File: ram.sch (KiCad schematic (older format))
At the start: 3 parts, among them U1 LFE5U-45F-6BG381C, U9 MT48LC4M16A2TG

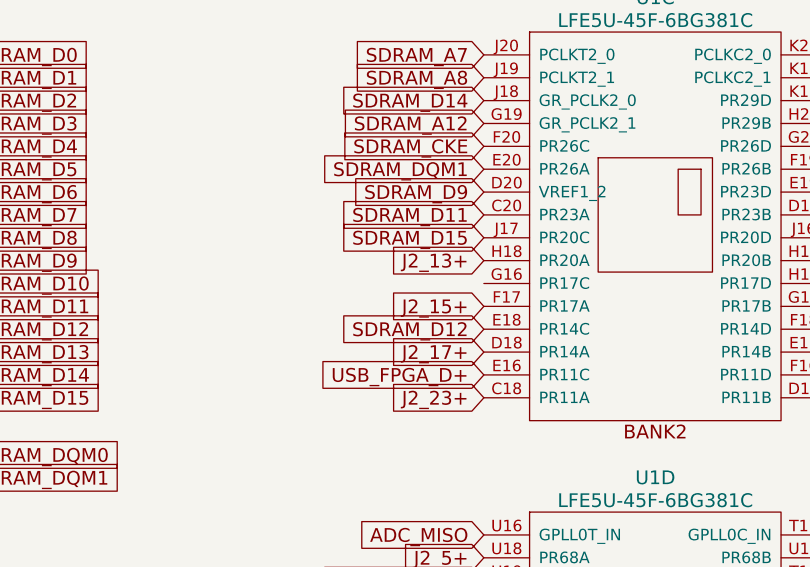
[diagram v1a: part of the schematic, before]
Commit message: schematics: connecting SHUTDOWN to FPGA
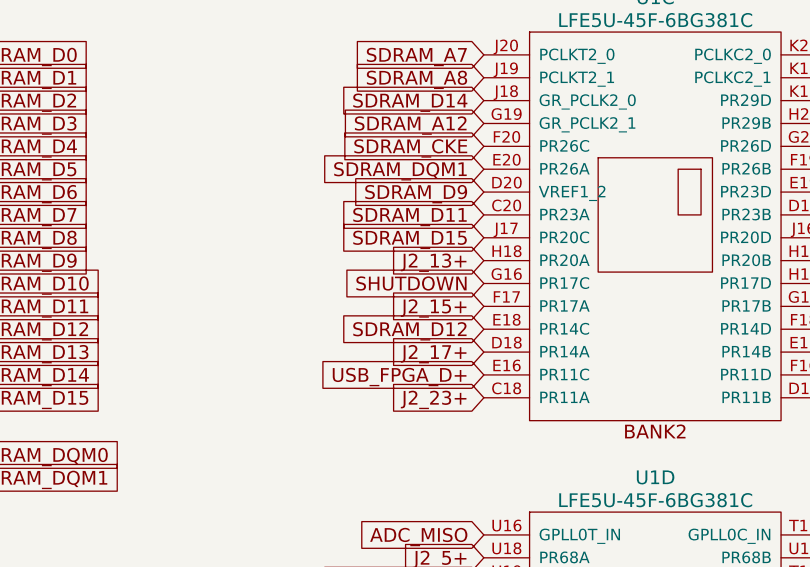
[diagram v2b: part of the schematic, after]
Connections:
- net SHUTDOWN: now reaches U1.G16 (PR17C)
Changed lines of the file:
@@
 	1    0    0    -1
 $EndComp
+Text GLabel 8550 3450 0    60   Input ~ 0
+SHUTDOWN
 $EndSCHEMATC

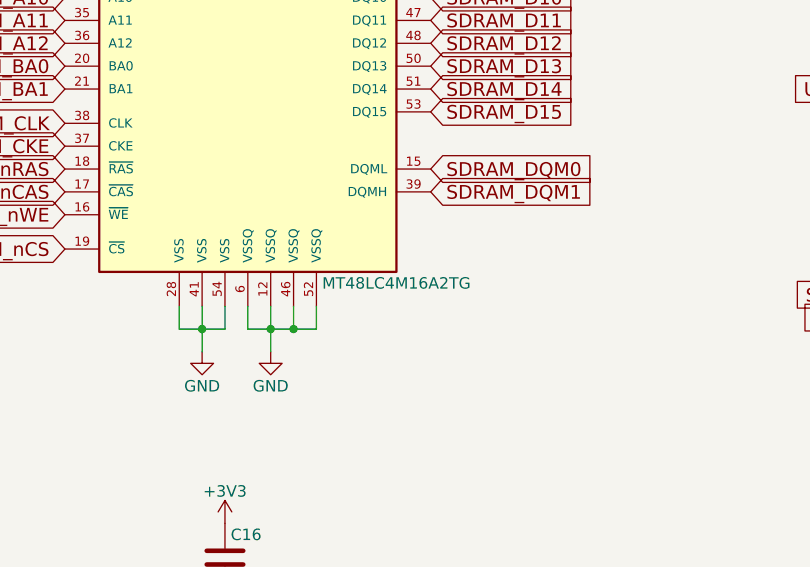
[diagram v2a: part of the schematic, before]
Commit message: schematics: corrected SDRAM part number
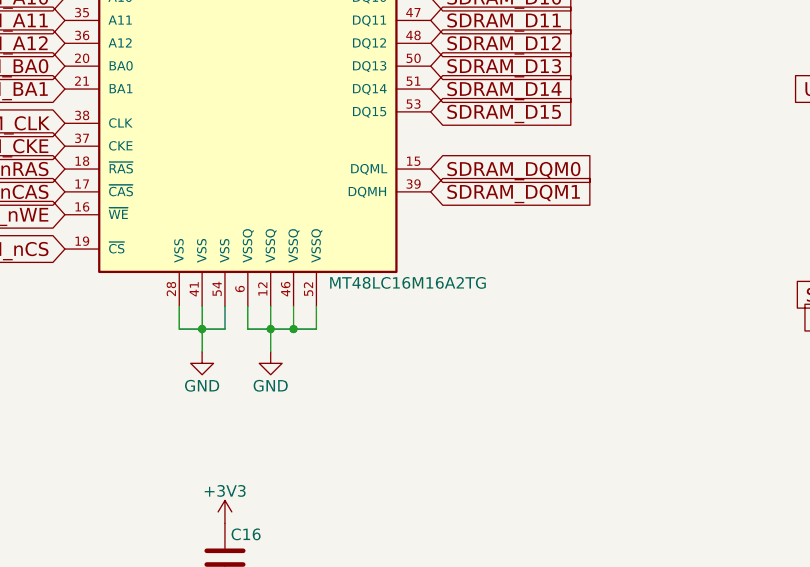
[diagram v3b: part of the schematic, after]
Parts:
- U9: value MT48LC4M16A2TG -> MT48LC16M16A2TG
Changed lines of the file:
@@
 AR Path="/58D6D507/5A04F49A" Ref="U2"  Part="1"
 F 0 "U2" H 4850 4700 50  0000 C CNN
-F 1 "MT48LC4M16A2TG" H 6100 2300 50  0000 C CNN
+F 1 "MT48LC16M16A2TG" H 6150 2300 50  0000 C CNN
 F 2 "TSOP54:TSOP54" H 5450 3500 50  0001 C CIN
 F 3 "https://www.micron.com/~/media/Documents/Products/Data%20Sheet/DRAM/256Mb_sdr.pdf" H 5450 3250 50  0001 C CNN

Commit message: schematics: SDRAM manufacturer url and PN
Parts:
- U9: Distributor1_PN (none) -> 913-4816M16A2TG6AGTR; MFG_PN (none) -> MT48LC16M16A2TG-7E; MFG_URL (none) -> www.micron.com
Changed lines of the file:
@@
 F 2 "TSOP54:TSOP54" H 5450 3500 50  0001 C CIN
 F 3 "https://www.micron.com/~/media/Documents/Products/Data%20Sheet/DRAM/256Mb_sdr.pdf" H 5450 3250 50  0001 C CNN
-F 4 "www.mouser.com" H 5450 3500 60  0001 C CNN "Distributor1_URL"
+F 4 "www.micron.com" H 5450 3500 60  0001 C CNN "MFG_URL"
+F 5 "MT48LC16M16A2TG-7E" H 5450 3500 60  0001 C CNN "MFG_PN"
+F 6 "www.mouser.com" H 5450 3500 60  0001 C CNN "Distributor1_URL"
+F 7 "913-4816M16A2TG6AGTR" H 5450 3500 60  0001 C CNN "Distributor1_PN"
 	1    5450 3500
 	1    0    0    -1

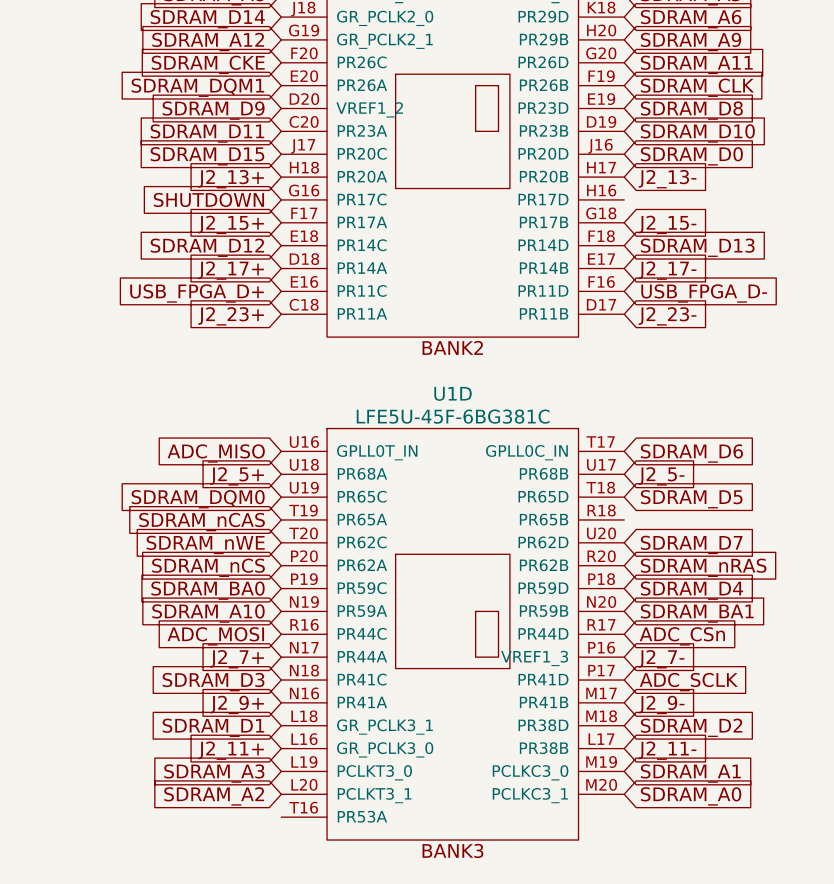
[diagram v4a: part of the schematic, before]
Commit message: schematics: renaming pins J..+- to GP,GN..
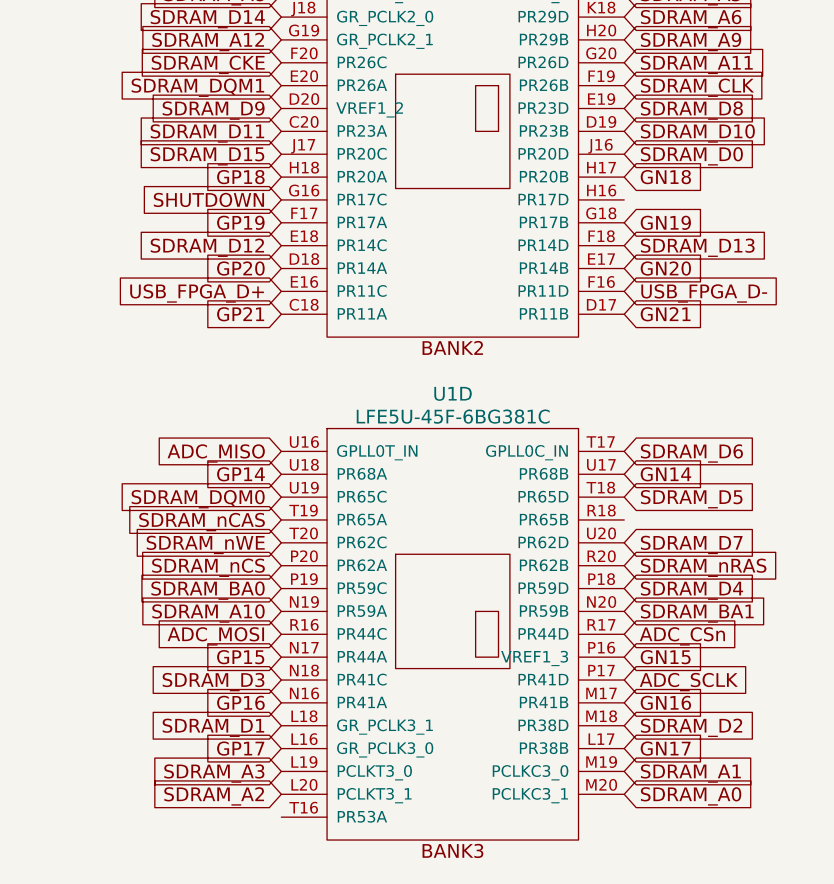
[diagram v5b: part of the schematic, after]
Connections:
- net J2_11+ renamed GP17
- net J2_11- renamed GN17
- net J2_13+ renamed GP18
- net J2_13- renamed GN18
- net J2_15+ renamed GP19
- net J2_15- renamed GN19
- net J2_17+ renamed GP20
- net J2_17- renamed GN20
- net J2_23+ renamed GP21
- net J2_23- renamed GN21
- net J2_5+ renamed GP14
- net J2_5- renamed GN14
- net J2_7+ renamed GP15
- net J2_7- renamed GN15
- net J2_9+ renamed GP16
- net J2_9- renamed GN16
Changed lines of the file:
@@
 Connection ~ 5250 2100
 $Comp
-L +3V3 #PWR0105
+L +3V3 #PWR0104
 U 1 1 58D928FF
 P 5250 2000
-F 0 "#PWR0105" H 5250 1850 50  0001 C CNN
+F 0 "#PWR0104" H 5250 1850 50  0001 C CNN
 F 1 "+3V3" H 5250 2140 50  0000 C CNN
 F 2 "" H 5250 2000 50  0000 C CNN
@@
 $EndComp
 $Comp
-L +3V3 #PWR0106
+L +3V3 #PWR0105
 U 1 1 58D92915
 P 5550 2000
-F 0 "#PWR0106" H 5550 1850 50  0001 C CNN
+F 0 "#PWR0105" H 5550 1850 50  0001 C CNN
 F 1 "+3V3" H 5550 2140 50  0000 C CNN
 F 2 "" H 5550 2000 50  0000 C CNN
@@
 Connection ~ 5650 4900
 $Comp
-L GND #PWR0107
+L GND #PWR0106
 U 1 1 58D929C8
 P 5250 5000
-F 0 "#PWR0107" H 5250 4750 50  0001 C CNN
+F 0 "#PWR0106" H 5250 4750 50  0001 C CNN
 F 1 "GND" H 5250 4850 50  0000 C CNN
 F 2 "" H 5250 5000 50  0000 C CNN
@@
 $EndComp
 $Comp
-L GND #PWR0108
+L GND #PWR0107
 U 1 1 58D929DE
 P 5550 5000
-F 0 "#PWR0108" H 5550 4750 50  0001 C CNN
+F 0 "#PWR0107" H 5550 4750 50  0001 C CNN
 F 1 "GND" H 5550 4850 50  0000 C CNN
 F 2 "" H 5550 5000 50  0000 C CNN
@@
 SDRAM_nCS
 Text GLabel 10050 4650 2    60   Input ~ 0
-J2_5-
+GN14
 Text GLabel 10050 5450 2    60   Input ~ 0
-J2_7-
+GN15
 Text GLabel 8550 5450 0    60   Input ~ 0
-J2_7+
+GP15
 Text GLabel 8550 4650 0    60   Input ~ 0
-J2_5+
+GP14
 Text GLabel 8550 5650 0    60   Input ~ 0
-J2_9+
+GP16
 Text GLabel 10050 5650 2    60   Input ~ 0
-J2_9-
+GN16
 Text GLabel 10050 3350 2    60   Input ~ 0
-J2_13-
+GN18
 Text GLabel 10050 3950 2    60   Input ~ 0
-J2_23-
+GN21
 Text GLabel 10050 3750 2    60   Input ~ 0
-J2_17-
+GN20
 Text GLabel 8550 3350 0    60   Input ~ 0
-J2_13+
+GP18
 Text GLabel 8550 3950 0    60   Input ~ 0
-J2_23+
+GP21
 Text GLabel 8550 3750 0    60   Input ~ 0
-J2_17+
+GP20
 Text GLabel 10050 3550 2    60   Input ~ 0
-J2_15-
+GN19
 Text GLabel 8550 3550 0    60   Input ~ 0
-J2_15+
+GP19
 Text GLabel 10050 5850 2    60   Input ~ 0
-J2_11-
+GN17
 Text GLabel 8550 5850 0    60   Input ~ 0
-J2_11+
+GP17
 $Comp
 L C C16
@@
 $EndComp
 $Comp
-L GND #PWR0109
+L GND #PWR0108
 U 1 1 59131FCA
 P 5350 6050
-F 0 "#PWR0109" H 5350 5800 50  0001 C CNN
+F 0 "#PWR0108" H 5350 5800 50  0001 C CNN
 F 1 "GND" H 5350 5900 50  0000 C CNN
 F 2 "" H 5350 6050 50  0000 C CNN
@@
 $EndComp
 $Comp
-L +3V3 #PWR0110
+L +3V3 #PWR0109
 U 1 1 59132092
 P 5350 5750
-F 0 "#PWR0110" H 5350 5600 50  0001 C CNN
+F 0 "#PWR0109" H 5350 5600 50  0001 C CNN
 F 1 "+3V3" H 5350 5890 50  0000 C CNN
 F 2 "" H 5350 5750 50  0000 C CNN

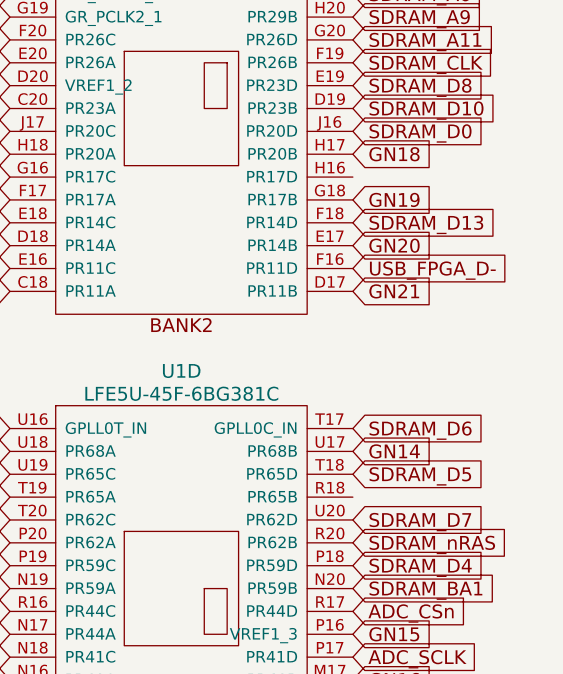
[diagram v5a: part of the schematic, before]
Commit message: schematics: routing FPGA to SPI QUAD. BTN_R,U connected to BANK2,3 on "ram" sheet
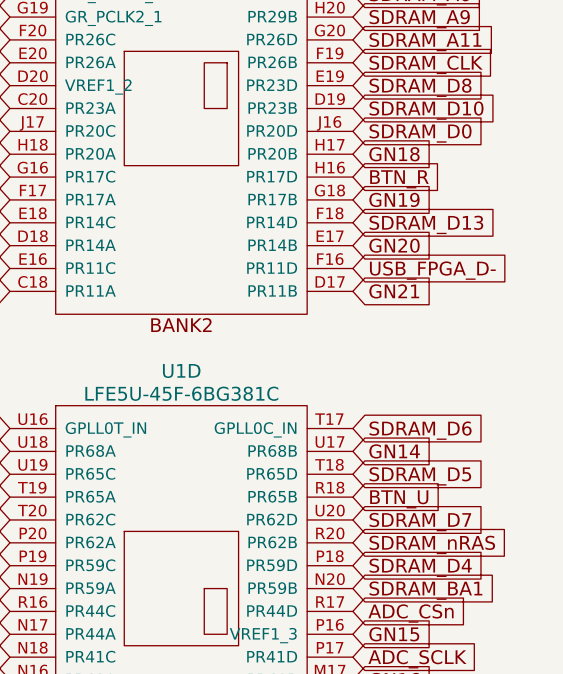
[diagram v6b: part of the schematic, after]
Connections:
- net BTN_R: now reaches U1.H16 (PR17D)
- net BTN_U: now reaches U1.R18 (PR65B)
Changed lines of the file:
@@
 Text GLabel 8550 3450 0    60   Input ~ 0
 SHUTDOWN
+Text GLabel 10050 4850 2    60   Input ~ 0
+BTN_U
+Text GLabel 10050 3450 2    60   Input ~ 0
+BTN_R
 $EndSCHEMATC

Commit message: footprints: FPGA renaming Quad SPI lines D2,D3 schematics: reference FPGA footprint directly (not from rescue file)
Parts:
- U1: symbol LFE5U-45F-6BG381C-RESCUE-ulx3s -> LFE5U-45F-6BG381C
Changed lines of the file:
@@
 SDRAM_A12
 $Comp
-L LFE5U-45F-6BG381C-RESCUE-ulx3s U1
+L LFE5U-45F-6BG381C U1
 U 3 1 5A07B063
 P 9300 3150
+AR Path="/5A07B063" Ref="U1"  Part="3"
+AR Path="/58D6D507/5A07B063" Ref="U1"  Part="3"
 F 0 "U1" H 9300 4100 60  0000 C CNN
 F 1 "LFE5U-45F-6BG381C" H 9300 4000 60  0000 C CNN
@@
 $EndComp
 $Comp
-L LFE5U-45F-6BG381C-RESCUE-ulx3s U1
+L LFE5U-45F-6BG381C U1
 U 4 1 5A07B0B9
 P 9300 5250
+AR Path="/5A07B0B9" Ref="U1"  Part="4"
+AR Path="/58D6D507/5A07B0B9" Ref="U1"  Part="4"
 F 0 "U1" H 9300 6200 60  0000 C CNN
 F 1 "LFE5U-45F-6BG381C" H 9300 6100 60  0000 C CNN

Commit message: schematics: cleanup of MFG_PN to simplify BOM
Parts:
- U1: MFG_PN (none) -> LFE5U-45F-6BG381C
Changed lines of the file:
@@
 F 2 "lfe5bg381:BGA-381_pitch0.8mm_dia0.4mm" H 8250 4100 60  0001 C CNN
 F 3 "http://www.latticesemi.com/~/media/LatticeSemi/Documents/DataSheets/ECP5/FPGA-DS-02012.pdf" H 8250 4100 60  0001 C CNN
-F 4 "www.mouser.com" H 9300 3150 60  0001 C CNN "Distributor1_URL"
+F 4 "LFE5U-45F-6BG381C" H 9300 3150 60  0001 C CNN "MFG_PN"
+F 5 "www.mouser.com" H 9300 3150 60  0001 C CNN "Distributor1_URL"
 	3    9300 3150
 	1    0    0    -1
@@
 F 2 "lfe5bg381:BGA-381_pitch0.8mm_dia0.4mm" H 8250 6200 60  0001 C CNN
 F 3 "http://www.latticesemi.com/~/media/LatticeSemi/Documents/DataSheets/ECP5/FPGA-DS-02012.pdf" H 8250 6200 60  0001 C CNN
-F 4 "www.mouser.com" H 9300 5250 60  0001 C CNN "Distributor1_URL"
+F 4 "LFE5U-45F-6BG381C" H 9300 5250 60  0001 C CNN "MFG_PN"
+F 5 "www.mouser.com" H 9300 5250 60  0001 C CNN "Distributor1_URL"
 	4    9300 5250
 	1    0    0    -1
